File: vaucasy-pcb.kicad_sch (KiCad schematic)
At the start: 1 part, among them U1 STM32F401RET6

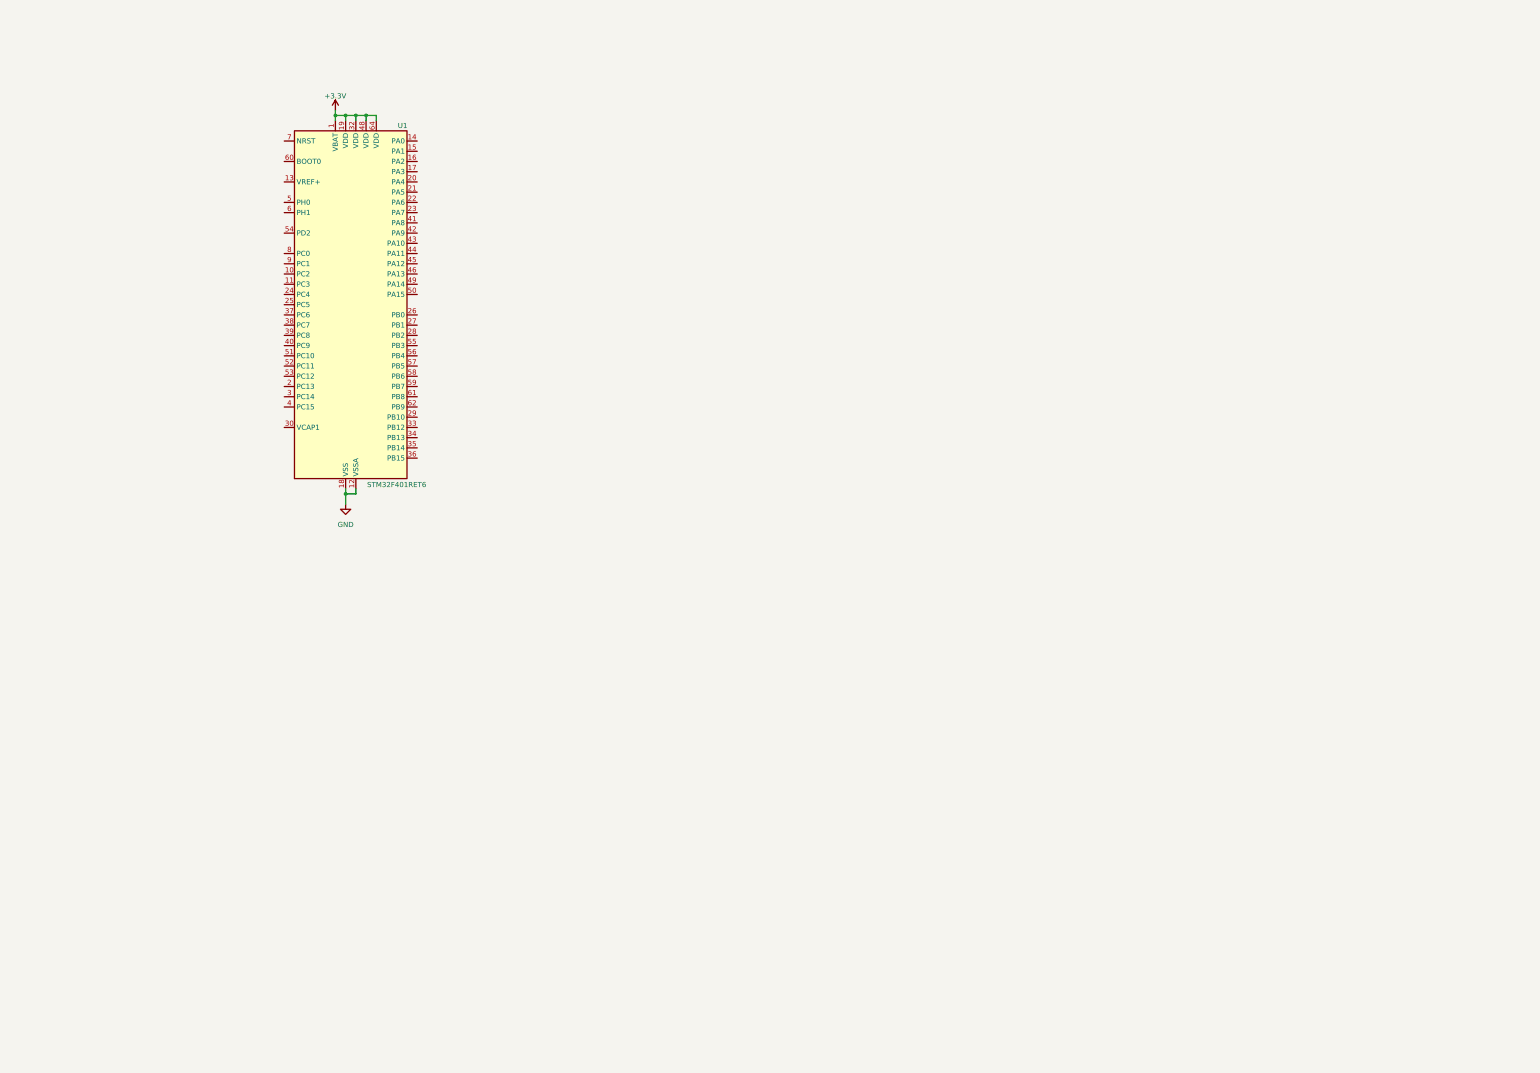
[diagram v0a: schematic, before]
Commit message: Switch matrix, connector and OLED added
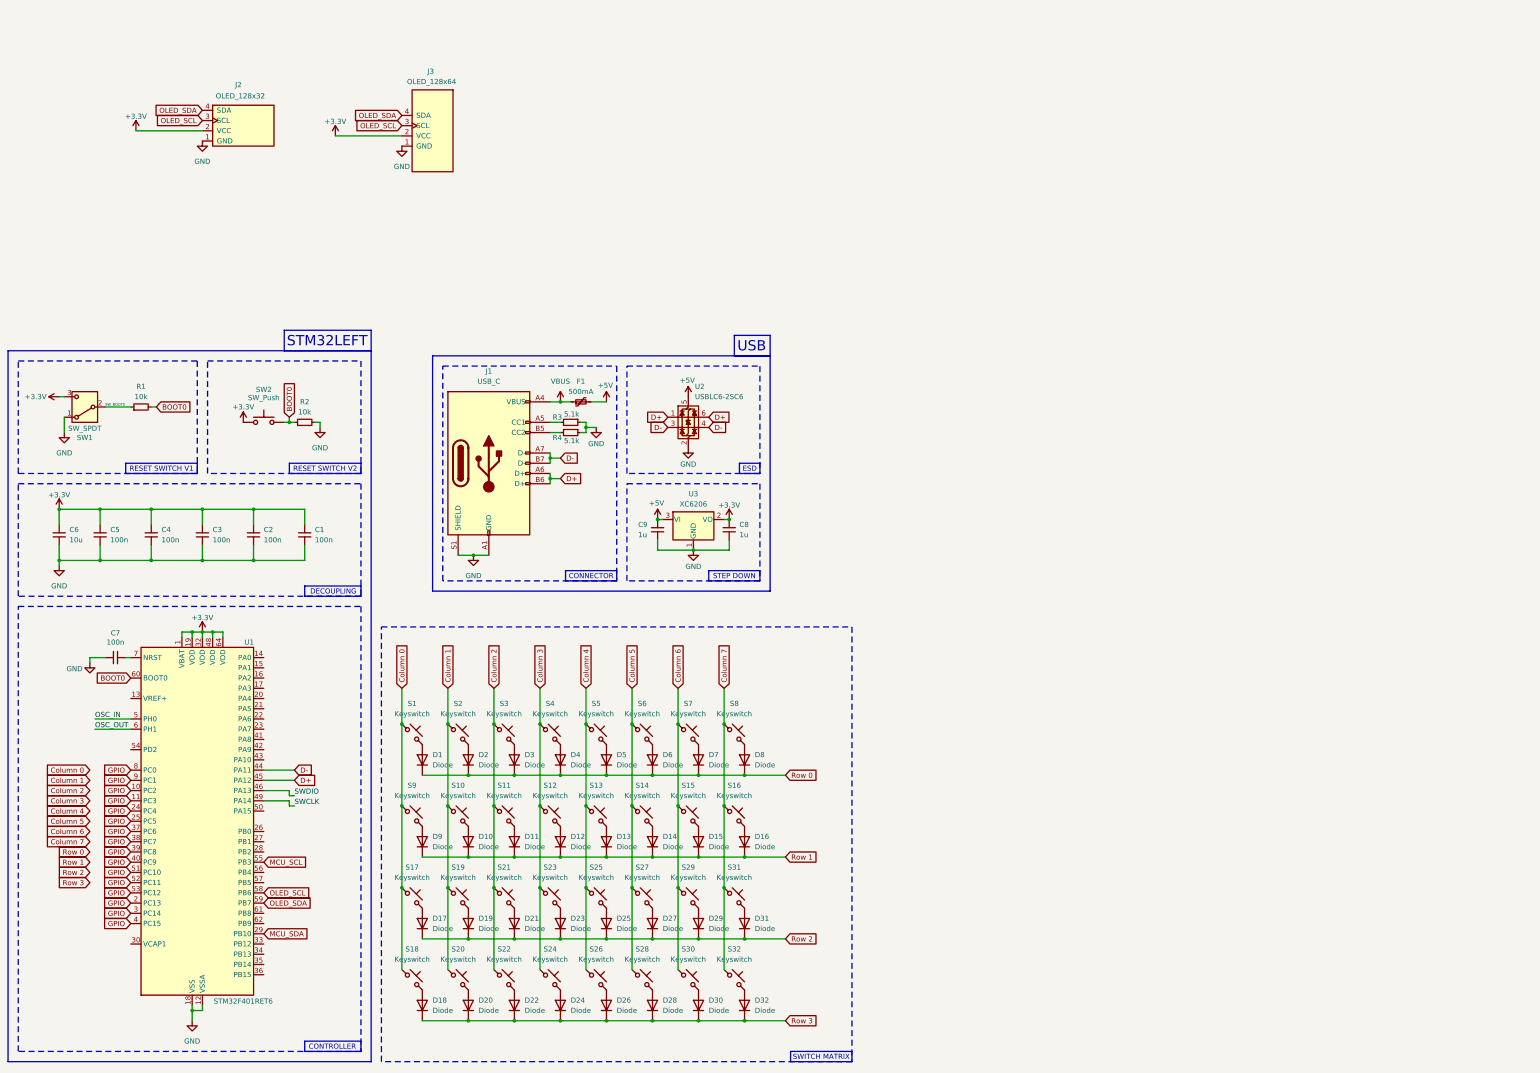
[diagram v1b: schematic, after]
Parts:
- added C1, C2, C3, C4, C5, C7: 100n, symbol Device:C_Small
- added C6: 10u, symbol Device:C_Small
- added C8, C9: 1u, symbol Device:C_Small
- added D1, D10, D11, D12, D13, D14, D15, D16, D17, D18, D19, D2, D20, D21, D22, D23, D24, D25, D26, D27, D28, D29, D3, D30, D31, D32, D4, D5, D6, D7, D8, D9: Diode, symbol ScottoKeebs:Placeholder_Diode
- added F1: 500mA, symbol Device:Polyfuse_Small
- added J1: USB_C, symbol Connector:USB_C_Receptacle_USB2.0_14P
- added J2: OLED_128x32, ScottoKeebs_Components:OLED_128x32, symbol ScottoKeebs:OLED_128x32
- added J3: OLED_128x64, ScottoKeebs_Components:OLED_128x64, symbol ScottoKeebs:OLED_128x64
- added R1, R2: 10k, symbol Device:R_Small
- added R3, R4: 5.1k, symbol Device:R_Small
- added S1, S10, S11, S12, S13, S14, S15, S16, S17, S18, S19, S2, S20, S21, S22, S23, S24, S25, S26, S27, S28, S29, S3, S30, S31, S32, S4, S5, S6, S7, S8, S9: Keyswitch, symbol ScottoKeebs:Placeholder_Keyswitch
- added SW1: SW_SPDT, symbol Switch:SW_SPDT
- added SW2: SW_Push, symbol Switch:SW_Push
- added U2: USBLC6-2SC6, Package_TO_SOT_SMD:SOT-23-6, symbol Power_Protection:USBLC6-2SC6
- added U3: XC6206, Package_TO_SOT_SMD:SOT-23-3, symbol Regulator_Linear:XC6206PxxxMR
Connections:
- net +3.3V: now also C1.2, C2.2, C3.2, C4.2, C5.2, C6.2, C8.2, J2.2 (VCC), J3.2 (VCC), SW1.3 (C), SW2.1, U3.2 (VO)
- net GND: now also C1.1, C2.1, C3.1, C4.1, C5.1, C6.1, C7.1, C8.1, C9.1, J1.A1 (GND), J1.A12 (GND), J1.B1 (GND), J1.B12 (GND), J1.S1 (SHIELD), J2.1 (GND), J3.1 (GND), R2.2, R3.1, R4.1, SW1.1 (A), U2.2 (GND), U3.1 (GND)
- net GPIO: now reaches U1.10 (PC2)
- net GPIO: now also U1.11 (PC3), U1.2 (PC13), U1.24 (PC4), U1.25 (PC5), U1.3 (PC14), U1.37 (PC6), U1.38 (PC7), U1.39 (PC8), U1.4 (PC15), U1.40 (PC9), U1.51 (PC10), U1.52 (PC11), U1.53 (PC12), U1.8 (PC0), U1.9 (PC1)
- net MCU_SDA: now reaches U1.29 (PB10)
- net D-: now reaches U1.44 (PA11)
- net D-: now also J1.A7 (D-), J1.B7 (D-), U2.3 (I/O2), U2.4 (I/O2)
- net D+: now reaches U1.45 (PA12)
- net D+: now also J1.A6 (D+), J1.B6 (D+), U2.1 (I/O1), U2.6 (I/O1)
- net SWDIO: now reaches U1.46 (PA13)
- net SWCLK: now reaches U1.49 (PA14)
- net OSC_IN: now reaches U1.5 (PH0)
- net MCU_SCL: now reaches U1.55 (PB3)
- net OLED_SCL: now reaches U1.58 (PB6)
- net OLED_SCL: now also J2.3 (SCL), J3.3 (SCL)
- net OLED_SDA: now reaches U1.59 (PB7)
- net OLED_SDA: now also J2.4 (SDA), J3.4 (SDA)
- net OSC_OUT: now reaches U1.6 (PH1)
- net BOOT0: now reaches U1.60 (BOOT0)
- net BOOT0: now also R1.2, R2.1, SW2.2
- net at U1.7 (NRST): now also C7.2
- new net: D29.2 (A), S29.2
- new net: D14.2 (A), S14.2
- new net: D6.2 (A), S6.2
- new net: D16.2 (A), S16.2
- new net: D1.2 (A), S1.2
- new net: D31.2 (A), S31.2
- new net: D12.2 (A), S12.2
- new net: D9.2 (A), S9.2
- new net: D27.2 (A), S27.2
- new net: D28.2 (A), S28.2
- new net: J1.A5 (CC1), R3.2
- new net: J1.B5 (CC2), R4.2
- new net: D25.2 (A), S25.2
- new net: D2.2 (A), S2.2
- new net: D7.2 (A), S7.2
- new net: D18.2 (A), S18.2
- new net: D4.2 (A), S4.2
- new net: D21.2 (A), S21.2
- new net: D11.2 (A), S11.2
- new net: D30.2 (A), S30.2
- new net: D15.2 (A), S15.2
- new net: D19.2 (A), S19.2
- new net: D32.2 (A), S32.2
- new net: D26.2 (A), S26.2
- new net: D24.2 (A), S24.2
- new net: D13.2 (A), S13.2
- new net: D8.2 (A), S8.2
- new net: D5.2 (A), S5.2
- new net: D17.2 (A), S17.2
- new net: D20.2 (A), S20.2
- new net: D22.2 (A), S22.2
- new net: D3.2 (A), S3.2
- new net: D23.2 (A), S23.2
- new net: D10.2 (A), S10.2
- new net +5V: C9.2, F1.2, U2.5 (VBUS), U3.3 (VI)
- new net Column 0: S1.1, S17.1, S18.1, S9.1
- new net Column 1: S10.1, S19.1, S2.1, S20.1
- new net Column 2: S11.1, S21.1, S22.1, S3.1
- new net Column 3: S12.1, S23.1, S24.1, S4.1
- new net Column 4: S13.1, S25.1, S26.1, S5.1
- new net Column 5: S14.1, S27.1, S28.1, S6.1
- new net Column 6: S15.1, S29.1, S30.1, S7.1
- new net Column 7: S16.1, S31.1, S32.1, S8.1
- new net Row 0: D1.1 (K), D2.1 (K), D3.1 (K), D4.1 (K), D5.1 (K), D6.1 (K), D7.1 (K), D8.1 (K)
- new net Row 1: D10.1 (K), D11.1 (K), D12.1 (K), D13.1 (K), D14.1 (K), D15.1 (K), D16.1 (K), D9.1 (K)
- new net Row 2: D17.1 (K), D19.1 (K), D21.1 (K), D23.1 (K), D25.1 (K), D27.1 (K), D29.1 (K), D31.1 (K)
- new net Row 3: D18.1 (K), D20.1 (K), D22.1 (K), D24.1 (K), D26.1 (K), D28.1 (K), D30.1 (K), D32.1 (K)
- new net SW_BOOT0: R1.1, SW1.2 (B)
- new net VBUS: F1.1, J1.A4 (VBUS), J1.A9 (VBUS), J1.B4 (VBUS), J1.B9 (VBUS)
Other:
- note added: "CONNECTOR"
- note added: "CONTROLLER"
- note added: "DECOUPLING"
- note added: "ESD"
- note added: "RESET SWITCH V1"
- note added: "RESET SWITCH V2"
- note added: "STEP DOWN"
- note added: "STM32LEFT"
- note added: "SWITCH MATRIX"
- note added: "USB"
- moved on the sheet: U1

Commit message: Schematic finished
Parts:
- added C10, C11: 8p, Capacitor_SMD:C_0402_1005Metric, symbol Device:C_Small
- added C12: 4.7uF, Capacitor_SMD:C_0603_1608Metric, symbol Device:C_Small
- added C13, C14, C15, C16: 100n, Capacitor_SMD:C_0402_1005Metric, symbol Device:C_Small
- added D33: Diode, ScottoKeebs_Components:Diode_SOD-123, symbol ScottoKeebs:Placeholder_Diode
- added J4: Trackball, Connector_PinHeader_2.54mm:PinHeader_1x05_P2.54mm_Vertical, symbol Connector_Generic:Conn_01x05
- added J5: HC-05 BT, Connector_PinHeader_2.54mm:PinHeader_1x06_P2.54mm_Vertical, symbol Connector_Generic:Conn_01x06
- added J6: DEBUG, Connector_PinHeader_2.54mm:PinHeader_1x04_P2.54mm_Vertical, symbol Connector:Conn_01x04_Pin
- added R10, R11, R12, R13, R14, R15, R16, R9: 4.7k, Resistor_SMD:R_0402_1005Metric, symbol Device:R_Small
- added R5, R6, R7, R8: 10k, Resistor_SMD:R_0402_1005Metric, symbol Device:R_Small
- added SW3: RotaryEncoder_Switch, Rotary_Encoder:RotaryEncoder_Alps_EC11E-Switch_Vertical_H20mm, symbol Device:RotaryEncoder_Switch
- added U4, U5: TRRS, ScottoKeebs_Components:TRRS_PJ-320A, symbol ScottoKeebs:Placeholder_TRRS
- added Y1: 8MHz, Crystal:Crystal_SMD_3225-4Pin_3.2x2.5mm, symbol Device:Crystal_GND24_Small
- C1, C2, C3, C4, C5, C7, C8, C9: footprint (none) -> Capacitor_SMD:C_0402_1005Metric
- C6: footprint (none) -> Capacitor_SMD:C_0603_1608Metric
- D1, D10, D11, D12, D13, D14, D15, D16, D17, D18, D19, D2, D20, D21, D22, D23, D24, D25, D26, D27, D28, D29, D3, D30, D31, D32, D4, D5, D6, D7, D8, D9: footprint (none) -> ScottoKeebs_Components:Diode_SOD-123
- F1: footprint (none) -> Fuse:Fuse_1206_3216Metric
- J1: footprint (none) -> Connector_USB:USB_C_Receptacle_GCT_USB4105-xx-A_16P_TopMnt_Horizontal
- R1, R2, R3, R4: footprint (none) -> Resistor_SMD:R_0402_1005Metric
- S1, S10, S11, S12, S13, S14, S15, S16, S17, S18, S19, S2, S20, S21, S22, S23, S24, S25, S26, S27, S28, S29, S3, S30, S31, S32, S4, S5, S6, S7, S8, S9: footprint (none) -> ScottoKeebs_Hotswap:Hotswap_Choc_V1V2_1.00u
- SW1: footprint (none) -> Button_Switch_THT:SW_Slide-03_Wuerth-WS-SLTV_10x2.5x6.4_P2.54mm
- SW2: footprint (none) -> Button_Switch_SMD:SW_Push_1P1T_XKB_TS-1187A
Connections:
- net +3.3V: now also U1.13 (VREF+), C13.2, J4.1 (Vcc), J6.4 (Pin_4), R10.1, R11.1, R12.2, R13.2, R14.1, R15.1, R16.2, R5.1, R9.2, U4.1 (SLEEVE), U5.1 (SLEEVE)
- net +5V: now also J5.5 (VCC)
- net Column 0: now also U1.8 (PC0)
- net Column 1: now also U1.9 (PC1)
- net Column 2: now also U1.10 (PC2)
- net Column 3: now also U1.11 (PC3)
- net Column 4: now also U1.24 (PC4)
- net Column 5: now also U1.25 (PC5)
- net Column 6: now also U1.37 (PC6)
- net Column 7: now also U1.38 (PC7)
- net GND: now also C10.1, C11.1, C12.2, C13.1, C14.1, C14.2, C15.1, C15.2, C16.2, D33.1 (K), J4.5 (GND), J5.4 (GND), J6.1 (Pin_1), R5.2, R7.1, R8.2, SW3.A, SW3.B, SW3.C, U4.2 (TIP), U5.2 (TIP), Y1.2, Y1.4
- net MCU_SCL: now also R15.2, U5.3 (RING1)
- net MCU_SDA: now also R16.1, U5.4 (RING2)
- net OLED_SCL: now also R12.1, R9.1
- net OLED_SDA: now also R10.2, R11.2
- net OSC_IN: now also C10.2, Y1.1
- net OSC_OUT: now also C11.2, Y1.3
- net Row 0: now also U1.53 (PC12)
- net Row 1: now also U1.2 (PC13)
- net Row 2: now also U1.3 (PC14)
- net Row 3: now also U1.4 (PC15)
- net SWCLK: now also J6.2 (Pin_2)
- net SWDIO: now also J6.3 (Pin_3)
- net MCU_NRST: now reaches C7.2, U1.7 (NRST)
- net UART2_TX: now reaches U1.16 (PA2)
- net UART2_TX: now also J5.3 (TXD)
- net UART2_RX: now reaches U1.17 (PA3)
- net UART2_RX: now also J5.2 (RXD)
- net MCU_VCAP1: now reaches U1.30 (VCAP1)
- net MCU_VCAP1: now also C12.1
- net ENCODER_A: now reaches U1.34 (PB13)
- net ENCODER_A: now also R8.1
- net ENCODER_B: now reaches U1.35 (PB14)
- net ENCODER_B: now also R7.2
- net ENCODER_PUSH: now reaches U1.36 (PB15)
- net ENCODER_PUSH: now also C16.1, R6.1
- net TRACK_SCL: now reaches U1.41 (PA8)
- net TRACK_SCL: now also J4.3 (SCL), R13.1
- net UART1_TX: now reaches U1.42 (PA9)
- net UART1_TX: now also U4.3 (RING1)
- net UART1_RX: now reaches U1.43 (PA10)
- net UART1_RX: now also U4.4 (RING2)
- removed net GPIO: U1.10 (PC2), U1.11 (PC3), U1.2 (PC13), U1.24 (PC4), U1.25 (PC5), U1.3 (PC14), U1.37 (PC6), U1.38 (PC7), U1.39 (PC8), U1.4 (PC15), U1.40 (PC9), U1.51 (PC10), U1.52 (PC11), U1.53 (PC12), U1.8 (PC0), U1.9 (PC1)
- new net: R6.2, SW3.S1
- new net: D33.2 (A), SW3.S2
- new net BT_EN: J5.6 (EN), U1.39 (PC8)
- new net TRACK_INT: J4.4 (INT), U1.51 (PC10)
- new net TRACK_SDA: J4.2 (SDA), R14.2, U1.40 (PC9)
- no-connect marks 0 -> 18
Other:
- note added: "2024.09.19."
- note added: "BLUETOOTH"
- note added: "Ergonomic split mechanical keyboard"
- note added: "I2C"
- note added: "OLED x32"
- note added: "OLED x64"
- note added: "OSCILLATOR"
- note added: "ROTARY ENCODER"
- note added: "TRACKBALL"
- note added: "TRRS CONNECTOR"
- note added: "UART"
- note added: "v1"
- moved on the sheet: C1, C2, C3, C4, C5, C6, C7, C8, C9, F1, J1, J2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

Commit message: Started PCB layout
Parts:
- SW1: footprint Button_Switch_THT:SW_Slide-03_Wuerth-WS-SLTV_10x2.5x6.4_P2.54mm -> Button_Switch_SMD:SW_SPDT_PCM12
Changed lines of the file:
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@@
 			)
 		)
-		(property "Footprint" "Button_Switch_THT:SW_Slide-03_Wuerth-WS-SLTV_10x2.5x6.4_P2.54mm"
+		(property "Footprint" "Button_Switch_SMD:SW_SPDT_PCM12"
 			(at 34.29 119.38 0)
 			(effects

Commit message: Left side finished
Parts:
- removed D32: Diode, ScottoKeebs_Components:Diode_SOD-123, symbol ScottoKeebs:Placeholder_Diode
- removed J3: OLED_128x64, ScottoKeebs_Components:OLED_128x64, symbol ScottoKeebs:OLED_128x64
- removed R11, R12, R15, R16: 4.7k, Resistor_SMD:R_0402_1005Metric, symbol Device:R_Small
- removed R5: 10k, Resistor_SMD:R_0402_1005Metric, symbol Device:R_Small
- removed S32: Keyswitch, ScottoKeebs_Hotswap:Hotswap_Choc_V1V2_1.00u, symbol ScottoKeebs:Placeholder_Keyswitch
- removed U5: TRRS, ScottoKeebs_Components:TRRS_PJ-320A, symbol ScottoKeebs:Placeholder_TRRS
- added C17: 100n, Capacitor_SMD:C_0402_1005Metric, symbol Device:C_Small
- J5: footprint Connector_PinHeader_2.54mm:PinHeader_1x06_P2.54mm_Vertical -> Connector_PinSocket_2.54mm:PinSocket_1x06_P2.54mm_Horizontal
- R2: value 10k -> 100R
- SW2: footprint Button_Switch_SMD:SW_Push_1P1T_XKB_TS-1187A -> ScottoKeebs_Components:Button_TL3342
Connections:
- net MCU_SCL is gone; now on net LColumn 2: U1.55 (PB3)
- net +3.3V: now also J5.5 (VCC); no longer SW2.1
- net +5V: no longer J5.5 (VCC)
- net GND: now also SW2.1, C17.2; no longer C14.2, C15.1, D33.1 (K), R2.2, R7.1, R8.2, SW3.A, SW3.B
- net LRow 3: now reaches U1.20 (PA4)
- net LRow 3: now also D18.1 (K), D20.1 (K), D22.1 (K), D24.1 (K), D26.1 (K), D28.1 (K), D30.1 (K)
- net LColumn 6: now reaches U1.21 (PA5)
- net LColumn 6: now also S15.1, S29.1, S30.1, S31.1, S7.1
- net LColumn 5: now reaches U1.22 (PA6)
- net LColumn 5: now also S14.1, S16.1, S27.1, S28.1, S6.1
- net LColumn 4: now reaches U1.23 (PA7)
- net LColumn 4: now also S13.1, S25.1, S26.1, S5.1, S8.1
- net LColumn 0: now reaches U1.28 (PB2)
- net LColumn 0: now also S1.1, S17.1, S18.1, S9.1
- net LRow 1: now reaches U1.54 (PD2)
- net LRow 1: now also D10.1 (K), D11.1 (K), D12.1 (K), D13.1 (K), D14.1 (K), D15.1 (K), D9.1 (K)
- net LColumn 3: now reaches U1.56 (PB4)
- net LColumn 3: now also C16.1, R6.1, S12.1, S23.1, S24.1, S4.1
- net LRow 2: now reaches U1.57 (PB5)
- net LRow 2: now also D17.1 (K), D19.1 (K), D21.1 (K), D23.1 (K), D25.1 (K), D27.1 (K), D29.1 (K)
- net BOOT0 renamed LBOOT0
- net LBOOT0: now also C17.1; no longer R2.1, SW2.2
- net BT_EN renamed LBT_EN
- removed net Column 0: S1.1, S17.1, S18.1, S9.1, U1.8 (PC0)
- net Column 1 renamed LColumn 1
- net LColumn 1: now also U1.53 (PC12); no longer U1.9 (PC1)
- net Column 2 renamed LColumn 2
- net LColumn 2: no longer U1.10 (PC2)
- removed net Column 3: S12.1, S23.1, S24.1, S4.1, U1.11 (PC3)
- removed net Column 4: S13.1, S25.1, S26.1, S5.1, U1.24 (PC4)
- removed net Column 5: S14.1, S27.1, S28.1, S6.1, U1.25 (PC5)
- removed net Column 6: S15.1, S29.1, S30.1, S7.1, U1.37 (PC6)
- removed net Column 7: S16.1, S31.1, S8.1, U1.38 (PC7)
- removed net D+: J1.A6 (D+), J1.B6 (D+), U1.45 (PA12), U2.1 (I/O1), U2.6 (I/O1)
- removed net D-: J1.A7 (D-), J1.B7 (D-), U1.44 (PA11), U2.3 (I/O2), U2.4 (I/O2)
- net ENCODER_A renamed LENCODER_A
- net ENCODER_B renamed LENCODER_B
- removed net ENCODER_PUSH: C16.1, R6.1, U1.36 (PB15)
- net MCU_NRST renamed LNRST
- net LNRST: now also R2.1
- net MCU_SDA renamed LRow 0
- net LRow 0: now also D1.1 (K), D2.1 (K), D3.1 (K), D4.1 (K), D5.1 (K), D6.1 (K), D7.1 (K)
- net MCU_VCAP1 renamed LMCU_VCAP1
- net OLED_SCL renamed LOLED_SCL
- net OLED_SDA renamed LOLED_SDA
- net OSC_IN renamed LOSC_IN
- net OSC_OUT renamed LOSC_OUT
- removed net Row 0: D1.1 (K), D2.1 (K), D3.1 (K), D4.1 (K), D5.1 (K), D6.1 (K), D7.1 (K), D8.1 (K), U1.53 (PC12)
- removed net Row 1: D10.1 (K), D11.1 (K), D12.1 (K), D13.1 (K), D14.1 (K), D15.1 (K), D16.1 (K), D9.1 (K), U1.2 (PC13)
- removed net Row 2: D17.1 (K), D19.1 (K), D21.1 (K), D23.1 (K), D25.1 (K), D27.1 (K), D29.1 (K), D31.1 (K), U1.3 (PC14)
- removed net Row 3: D18.1 (K), D20.1 (K), D22.1 (K), D24.1 (K), D26.1 (K), D28.1 (K), D30.1 (K), U1.4 (PC15)
- net SWCLK renamed LSWCLK
- net SWDIO renamed LSWDIO
- net TRACK_INT renamed LTRACK_INT
- net TRACK_SCL renamed LTRACK_SCL
- net TRACK_SDA renamed LTRACK_SDA
- net UART1_RX renamed LUART1_RX
- net UART1_TX renamed LUART1_TX
- net UART2_RX renamed LUART2_RX
- net UART2_TX renamed LUART2_TX
- new net: C15.1, R8.2, SW3.A
- new net: C14.2, R7.1, SW3.B
- new net: R2.2, SW2.2
- new net LD+: J1.A6 (D+), J1.B6 (D+), U2.3 (I/O2)
- new net LD-: J1.A7 (D-), J1.B7 (D-), U2.1 (I/O1)
- new net LROW4: D16.1 (K), D31.1 (K), D8.1 (K)
- new net LRow 4: D33.1 (K), U1.10 (PC2)
- new net LsD+: U1.45 (PA12), U2.4 (I/O2)
- new net LsD-: U1.44 (PA11), U2.6 (I/O1)
- no-connect marks 18 -> 21
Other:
- note added: "LEFT SWITCH MATRIX"
- note removed: "2024.09.19."
- note removed: "Ergonomic split mechanical keyboard"
- note removed: "I2C"
- note removed: "OLED x64"
- note removed: "RESET SWITCH V2"
- note removed: "SWITCH MATRIX"
- note removed: "TRRS CONNECTOR"
- note removed: "v1"
- moved on the sheet: C14, C15, C16, C8, C9, D1, D10, D11, D12, D13, D14, D15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
